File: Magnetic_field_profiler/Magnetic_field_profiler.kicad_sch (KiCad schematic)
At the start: 72 parts, among them J1 USB_B_Micro, J2 Screw_Terminal_01x02, J3 Conn_01x04_Socket, J4 Conn_01x04_Socket, Q1 BSS123, SW1 SW_SPDT, U1 STM32F103C8Tx, U2 TP6841S6, U3 MCP23S17, U4 DRV8825, U5 DRV8825, Y1 Crystal_GND24

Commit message: Adding part descriptions
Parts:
- C13, C15: footprint Capacitor_SMD:C_0603_1608Metric -> Capacitor_SMD:C_0805_2012Metric
- FB1: Distributor Link (none) -> https://www.digikey.com/en/products/detail/murata-electroni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; Manufacturer (none) -> Murata Electronics; Manufacturer Part Number (none) -> BLM18KG121TN1D
- J2: Distributor Link (none) -> https://www.digikey.com/en/products/detail/phoenix-contact/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; Manufacturer (none) -> Phoenix Contact; Manufacturer Part Number (none) -> 1715022
- L1: footprint Inductor_SMD:L_0603_1608Metric -> LED_SMD:LED_1210_3225Metric; Distributor Link (none) -> https://www.digikey.com/en/products/detail/taiyo-yuden/CBC3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; Manufacturer (none) -> Taiyo Yuden; Manufacturer Part Number (none) -> CBC3225T101MR
- Q1: Distributor Link (none) -> https://www.digikey.com/en/products/detail/diodes-incorpora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; Manufacturer (none) -> Diodes Incorporated; Manufacturer Part Number (none) -> BSS123-7-F
- R18, R19, R20, R21: footprint Resistor_SMD:R_0402_1005Metric -> Resistor_SMD:R_1206_3216Metric; Distributor Link (none) -> https://www.digikey.com/en/products/detail/stackpole-electr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; Manufacturer (none) -> Stackpole Electronics Inc; Manufacturer Part Number (none) -> CSR1206FKR200
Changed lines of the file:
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@@
 			)
 		)
-		(property "Distributor Link" ""
+		(property "Distributor Link" "https://www.digikey.com/en/products/detail/phoenix-contact/1715022/260626"
+			(at 154.94 161.29 0)
+			(effects
+				(font
+					(size 1.27 1.27)
+				)
+				(hide yes)
+			)
+		)
+		(property "Manufacturer" "Phoenix Contact"
+			(at 154.94 161.29 0)
+			(effects
+				(font
+					(size 1.27 1.27)
+				)
+				(hide yes)
+			)
+		)
+		(property "Manufacturer Part Number" "1715022"
 			(at 154.94 161.29 0)
 			(effects
@@
 			)
 		)
-		(property "Manufacturer" ""
+		(property "Manufacturer" "Diodes Incorporated"
 			(at 234.95 163.83 0)
 			(effects
@@
 			)
 		)
-		(property "Manufacturer Part Number" ""
+		(property "Manufacturer Part Number" "BSS123-7-F"
 			(at 234.95 163.83 0)
 			(effects
@@
 			)
 		)
-		(property "Distributor Link" ""
+		(property "Distributor Link" "https://www.digikey.com/en/products/detail/diodes-incorporated/BSS123-7-F/717722"
 			(at 234.95 163.83 0)
 			(effects
@@
 			)
 		)
-		(property "Footprint" "Resistor_SMD:R_0402_1005Metric"
+		(property "Footprint" "Resistor_SMD:R_1206_3216Metric"
 			(at 110.49 247.142 90)
 			(effects
@@
 			)
 		)
-		(property "Manufacturer" ""
+		(property "Manufacturer" "Stackpole Electronics Inc"
 			(at 110.49 248.92 0)
 			(effects
@@
 			)
 		)
-		(property "Manufacturer Part Number" ""
+		(property "Manufacturer Part Number" "CSR1206FKR200"
 			(at 110.49 248.92 0)
 			(effects
@@
 			)
 		)
-		(property "Distributor Link" ""
+		(property "Distributor Link" "https://www.digikey.com/en/products/detail/stackpole-electronics-inc/CSR1206FKR200/1742391"
 			(at 110.49 248.92 0)
 			(effects
@@
 			)
 		)
-		(property "Footprint" "Inductor_SMD:L_0603_1608Metric"
+		(property "Footprint" "LED_SMD:LED_1210_3225Metric"
 			(at 95.25 161.29 0)
 			(effects
@@
 			)
 		)
-		(property "Manufacturer" ""
+		(property "Manufacturer" "Taiyo Yuden"
 			(at 95.25 161.29 0)
 			(effects
@@
 			)
 		)
-		(property "Manufacturer Part Number" ""
+		(property "Manufacturer Part Number" "CBC3225T101MR"
 			(at 95.25 161.29 0)
 			(effects
@@
 			)
 		)
-		(property "Distributor Link" ""
+		(property "Distributor Link" "https://www.digikey.com/en/products/detail/taiyo-yuden/CBC3225T101MR/958010"
 			(at 95.25 161.29 0)
 			(effects
@@
 			)
 		)
-		(property "Footprint" "Capacitor_SMD:C_0603_1608Metric"
+		(property "Footprint" "Capacitor_SMD:C_0805_2012Metric"
 			(at 111.4552 168.91 0)
 			(effects
@@
 			)
 		)
-		(property "Footprint" "Capacitor_SMD:C_0603_1608Metric"
+		(property "Footprint" "Capacitor_SMD:C_0805_2012Metric"
 			(at 32.7152 165.1 0)
 			(effects
@@
 			)
 		)
-		(property "Footprint" "Resistor_SMD:R_0402_1005Metric"
+		(property "Footprint" "Resistor_SMD:R_1206_3216Metric"
 			(at 110.49 248.158 90)
 			(effects
@@
 			)
 		)
-		(property "Manufacturer" ""
+		(property "Manufacturer" "Stackpole Electronics Inc"
 			(at 110.49 246.38 0)
 			(effects
@@
 			)
 		)
-		(property "Manufacturer Part Number" ""
+		(property "Manufacturer Part Number" "CSR1206FKR200"
 			(at 110.49 246.38 0)
 			(effects
@@
 			)
 		)
-		(property "Distributor Link" ""
+		(property "Distributor Link" "https://www.digikey.com/en/products/detail/stackpole-electronics-inc/CSR1206FKR200/1742391"
 			(at 110.49 246.38 0)
 			(effects
@@
 			)
 		)
-		(property "Footprint" "Resistor_SMD:R_0402_1005Metric"
+		(property "Footprint" "Resistor_SMD:R_1206_3216Metric"
 			(at 243.84 247.142 90)
 			(effects
@@
 			)
 		)
-		(property "Manufacturer" ""
+		(property "Manufacturer" "Stackpole Electronics Inc"
 			(at 243.84 248.92 0)
 			(effects
@@
 			)
 		)
-		(property "Manufacturer Part Number" ""
+		(property "Manufacturer Part Number" "CSR1206FKR200"
 			(at 243.84 248.92 0)
 			(effects
@@
 			)
 		)
-		(property "Distributor Link" ""
+		(property "Distributor Link" "https://www.digikey.com/en/products/detail/stackpole-electronics-inc/CSR1206FKR200/1742391"
 			(at 243.84 248.92 0)
 			(effects
@@
 			)
 		)
-		(property "Footprint" "Resistor_SMD:R_0402_1005Metric"
+		(property "Footprint" "Resistor_SMD:R_1206_3216Metric"
 			(at 243.84 248.158 90)
 			(effects
@@
 			)
 		)
-		(property "Manufacturer" ""
+		(property "Manufacturer" "Stackpole Electronics Inc"
 			(at 243.84 246.38 0)
 			(effects
@@
 			)
 		)
-		(property "Manufacturer Part Number" ""
+		(property "Manufacturer Part Number" "CSR1206FKR200"
 			(at 243.84 246.38 0)
 			(effects
@@
 			)
 		)
-		(property "Distributor Link" ""
+		(property "Distributor Link" "https://www.digikey.com/en/products/detail/stackpole-electronics-inc/CSR1206FKR200/1742391"
 			(at 243.84 246.38 0)
 			(effects
@@
 			)
 		)
-		(property "Manufacturer" ""
+		(property "Manufacturer" "Murata Electronics"
 			(at 152.4 33.02 0)
 			(effects
@@
 			)
 		)
-		(property "Manufacturer Part Number" ""
+		(property "Manufacturer Part Number" "BLM18KG121TN1D"
 			(at 152.4 33.02 0)
 			(effects
@@
 			)
 		)
-		(property "Distributor Link" ""
+		(property "Distributor Link" "https://www.digikey.com/en/products/detail/murata-electronics/BLM18KG121TN1D/1982762"
 			(at 152.4 33.02 0)
 			(effects

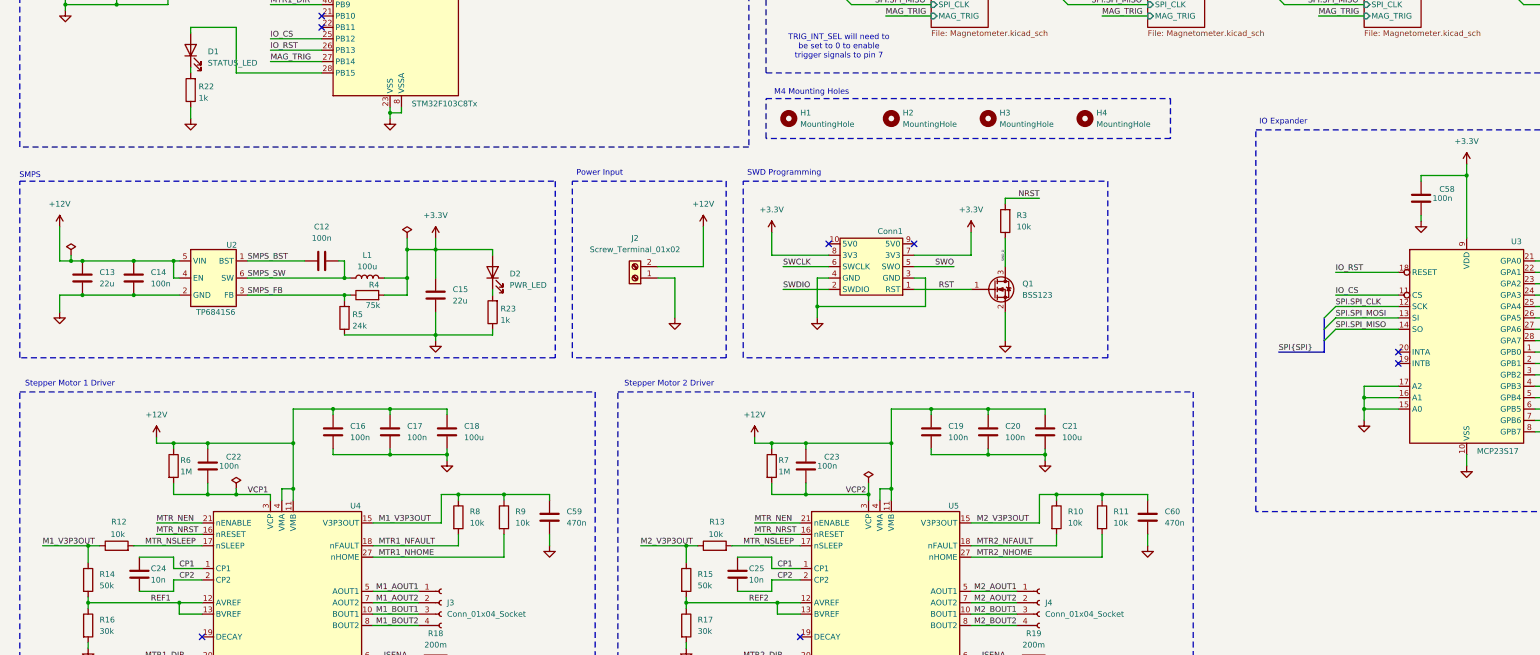
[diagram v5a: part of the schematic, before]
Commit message: DC-DC converter rework
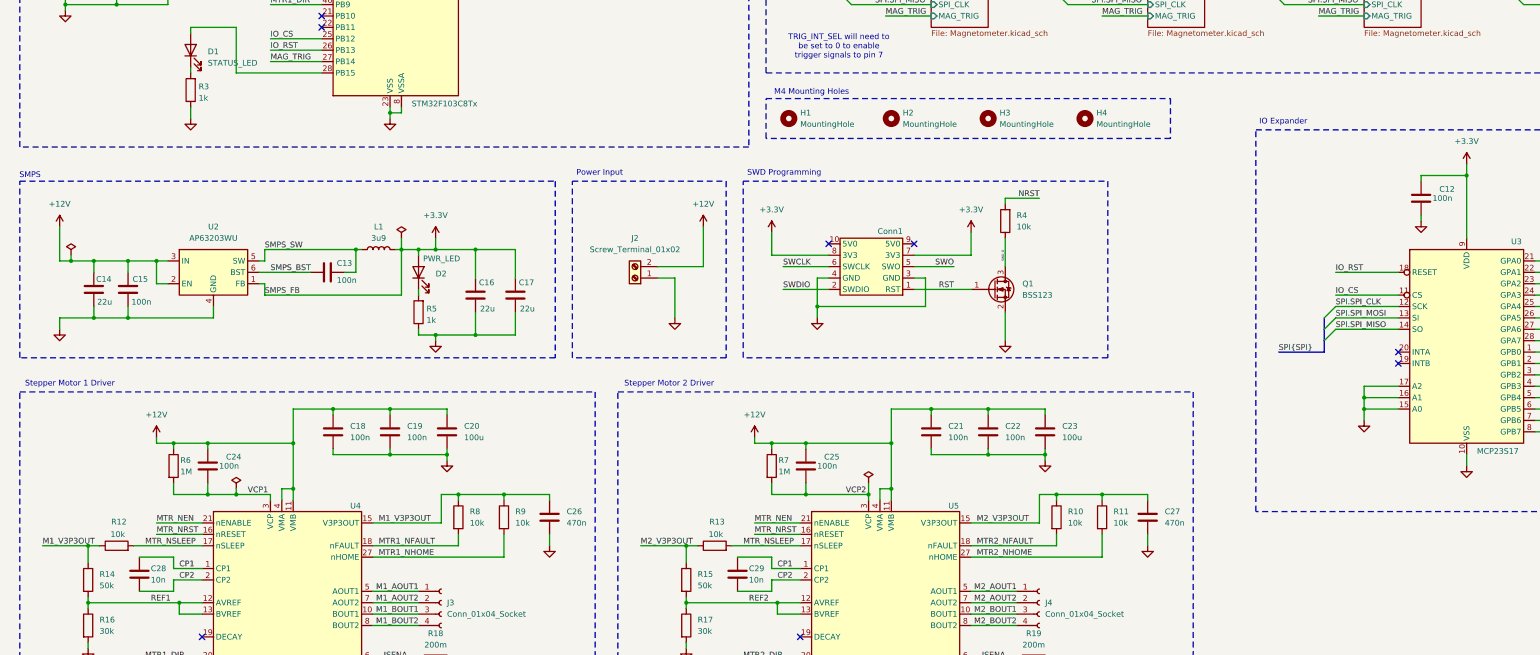
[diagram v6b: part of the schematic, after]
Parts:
- removed R4: 75k, Resistor_SMD:R_0402_1005Metric, symbol Device:R
- removed R5: 24k, Resistor_SMD:R_0402_1005Metric, symbol Device:R
- removed U2: TP6841S6, Package_TO_SOT_SMD:SOT-23-6, symbol Mag_Profiler_ICs:TP6841S6
- added C17: 22u, Capacitor_SMD:C_0805_2012Metric, symbol Device:C
- added U2: AP63203WU, Package_TO_SOT_SMD:TSOT-23-6, symbol Regulator_Switching:AP63203WU
- L1: value 100u -> 3u9; footprint LED_SMD:LED_1210_3225Metric -> Inductor_SMD:L_Abracon_ASPI-3012S; Distributor Link https://www.digikey.com/en/products/detail/taiyo-yuden/CBC3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 -> https://www.mouser.com/ProductDetail/ABRACON/ASPI-3012S-3R9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; Manufacturer Taiyo Yuden -> ABRACON; Manufacturer Part Number CBC3225T101MR -> ASPI-3012S-3R9N-T
- renumbered C58 to C12, C12 to C13, C13 to C14, C14 to C15, C15 to C16, C16 to C18, C17 to C19, C18 to C20, C19 to C21, C20 to C22, C21 to C23, C22 to C24, C23 to C25, C59 to C26, C60 to C27, C24 to C28, C25 to C29, R22 to R3, R3 to R4, R23 to R5
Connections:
- net +12V: now also C14.2, U2.2 (EN), U2.3 (IN); no longer C14.1
- net +3.3V: now also C17.1, U2.1 (FB)
- net GND: now also C14.1, C17.2, U2.4 (GND); no longer C14.2
- net SMPS_BST: now also U2.6 (BST)
- net SMPS_SW: now also U2.5 (SW)
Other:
- moved on the sheet: C13, C14, C15, C16, D2, L1, R5

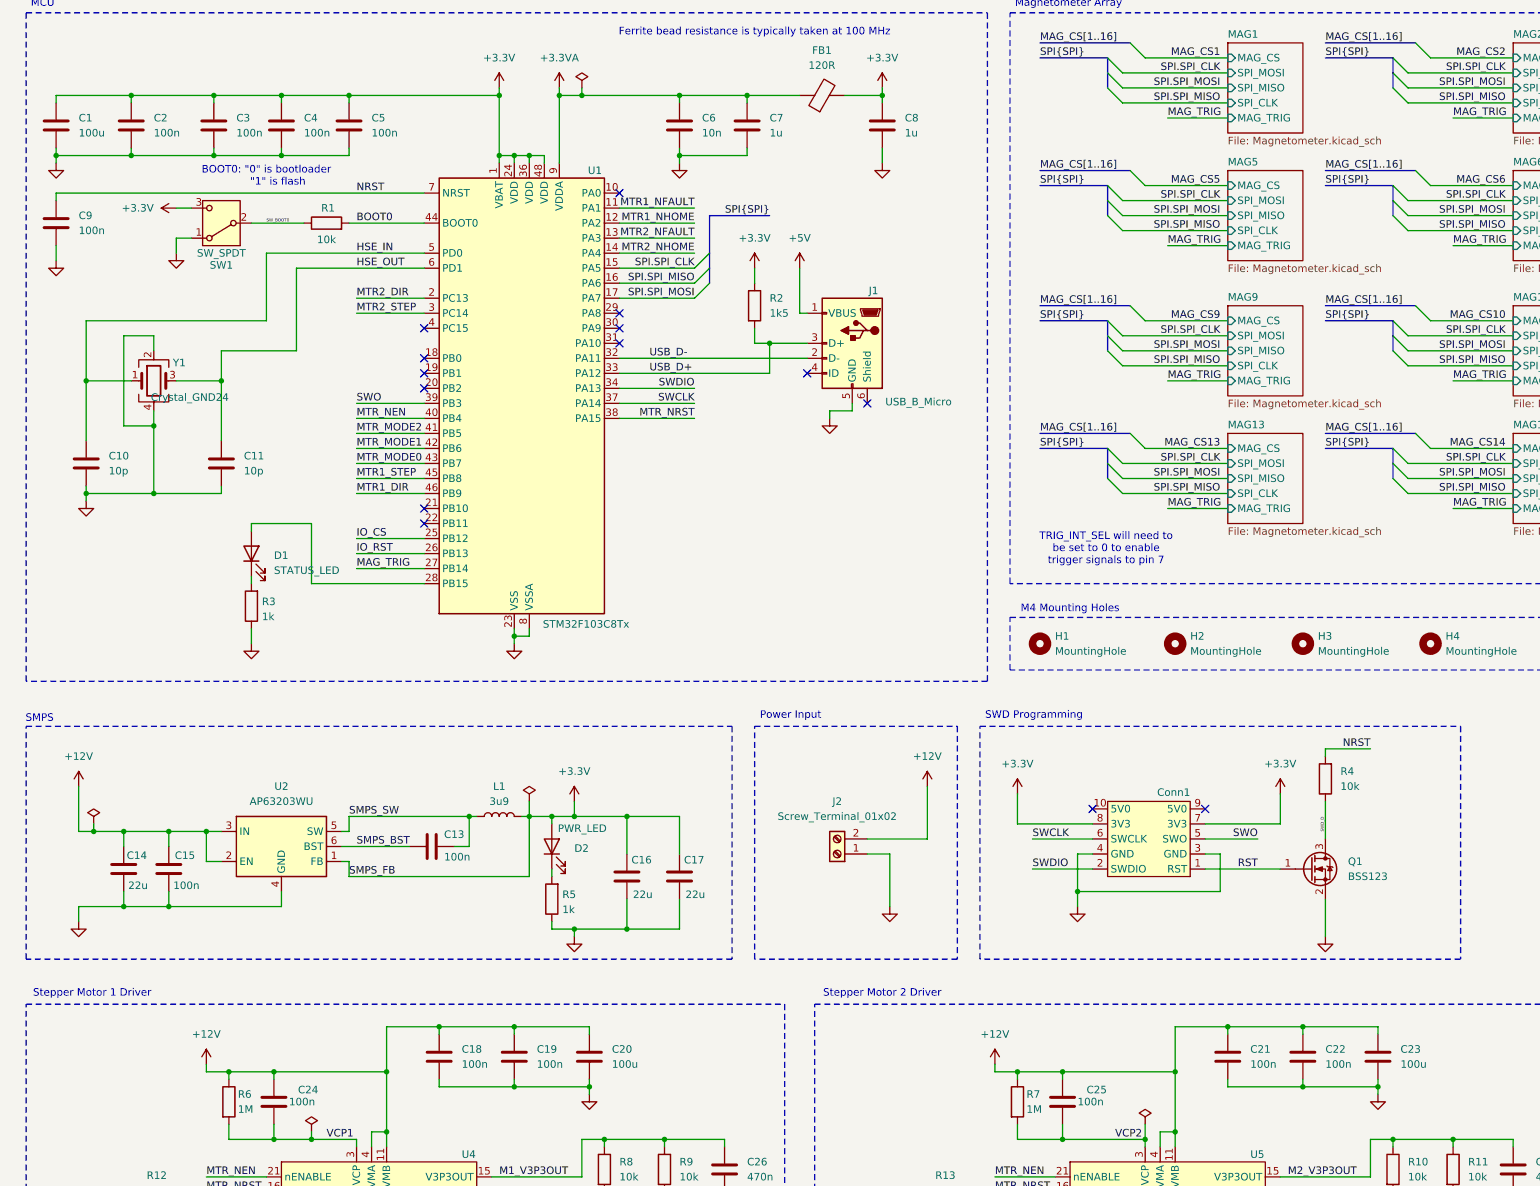
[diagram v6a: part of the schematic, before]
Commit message: Continued adding component description and sourcing information
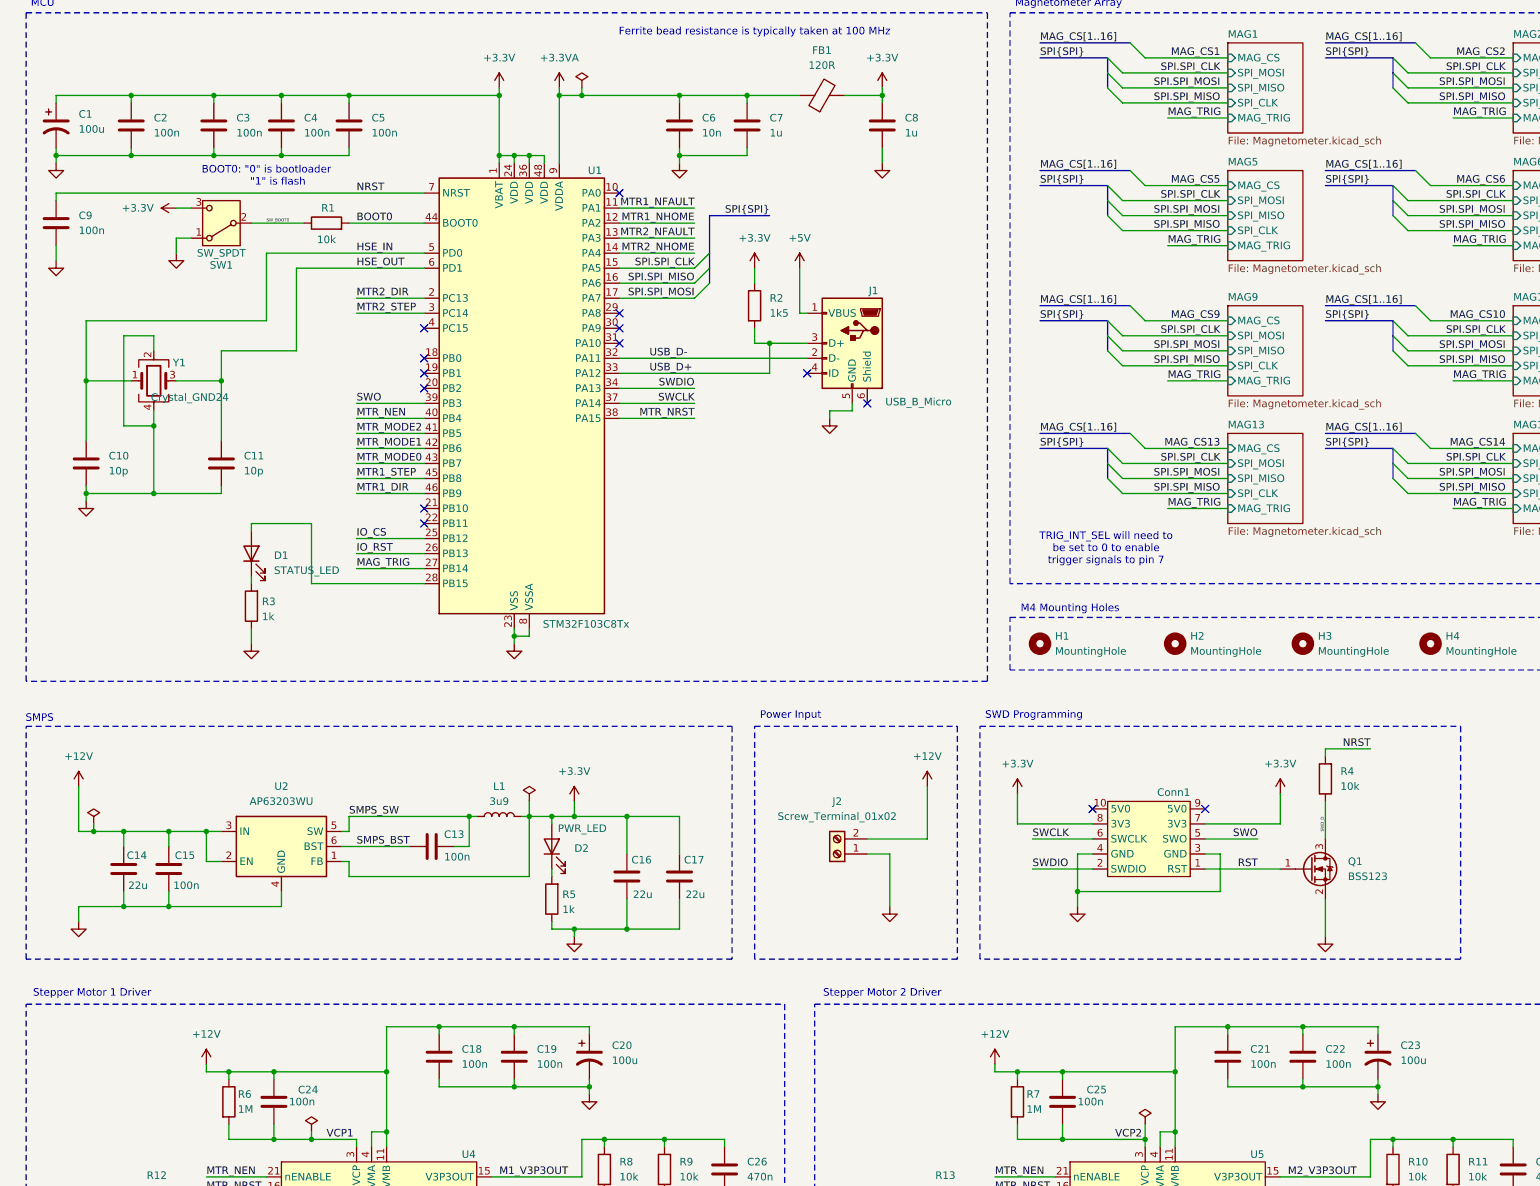
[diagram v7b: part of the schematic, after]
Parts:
- removed C1, C20, C23: 100u, Capacitor_SMD:C_0805_2012Metric, symbol Device:C
- added C1, C20, C23: 100u, Capacitor_THT:CP_Radial_D5.0mm_P2.00mm, symbol Device:C_Polarized_US
- C10, C11: Manufacturer (none) -> Murata Electronics; Manufacturer Part Number (none) -> GRM1555C1H100FA01D
- C12, C13, C15, C18, C19, C2, C21, C22, C24, C25, C3, C4, C5, C9: footprint Capacitor_SMD:C_0402_1005Metric -> Capacitor_SMD:C_0201_0603Metric; Distributor Link (none) -> https://www.digikey.com/en/products/detail/murata-electroni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; Manufacturer (none) -> Murata Electronics; Manufacturer Part Number (none) -> GRM033C81E104KE14D
- C14, C16, C17: footprint Capacitor_SMD:C_0805_2012Metric -> Capacitor_SMD:C_1206_3216Metric; Distributor Link (none) -> https://www.digikey.com/en/products/detail/samsung-electro-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; Manufacturer (none) -> Samsung Electro-Mechanics; Manufacturer Part Number (none) -> CL31A226MOCLNNC
- C26, C27: Distributor Link (none) -> https://www.digikey.com/en/products/detail/samsung-electro-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; Manufacturer (none) -> Samsung Electro-Mechanics; Manufacturer Part Number (none) -> CL21B474KAFNNNG
- C28, C29, C6: footprint Capacitor_SMD:C_0402_1005Metric -> Capacitor_SMD:C_0201_0603Metric; Distributor Link (none) -> https://www.digikey.com/en/products/detail/murata-electroni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; Manufacturer (none) -> Murata Electronics; Manufacturer Part Number (none) -> GRM033R61E103KA12D
- C7, C8: Distributor Link (none) -> https://www.digikey.com/en/products/detail/yageo/CC0603KRX5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; Manufacturer (none) -> YAGEO; Manufacturer Part Number (none) -> CC0603KRX5R8BB105
- R1, R10, R11, R12, R13, R4, R8, R9: footprint Resistor_SMD:R_0402_1005Metric -> Resistor_SMD:R_0805_2012Metric; Distributor Link (none) -> https://www.digikey.com/en/products/detail/stackpole-electr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; Manufacturer (none) -> Stackpole Electronics Inc; Manufacturer Part Number (none) -> RMCF0805JT10K0
- R14, R15: Distributor Link (none) -> https://www.digikey.com/en/products/detail/vishay-dale/CRCW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; Manufacturer (none) -> Vishay Dale; Manufacturer Part Number (none) -> CRCW040250K0FKED
- R16, R17: Distributor Link (none) -> https://www.digikey.com/en/products/detail/yageo/RC0402FR-0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; Manufacturer (none) -> YAGEO; Manufacturer Part Number (none) -> RC0402FR-0730KL
- R2: Distributor Link (none) -> https://www.digikey.com/en/products/detail/yageo/RC0805JR-0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; Manufacturer (none) -> YAGEO; Manufacturer Part Number (none) -> RC0805JR-071K5L
- R3, R5: Distributor Link (none) -> https://www.digikey.com/en/products/detail/yageo/RC0805FR-0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; Manufacturer (none) -> YAGEO; Manufacturer Part Number (none) -> RC0805FR-071KL
- R6, R7: Distributor Link (none) -> https://www.digikey.com/en/products/detail/te-connectivity-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; Manufacturer (none) -> TE Connectivity Passive Product; Manufacturer Part Number (none) -> CRGCQ0402J1M0
- U2: Distributor Link (none) -> https://www.digikey.com/en/products/detail/diodes-incorpora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; Manufacturer (none) -> Diodes Incorporated; Manufacturer Part Number (none) -> AP63203WU-7
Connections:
- net +12V: now also C20.1, C23.1
- net +3.3V: now also C1.1
- net GND: now also C1.2, C20.2, C23.2
